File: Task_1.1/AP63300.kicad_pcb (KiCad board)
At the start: 2 copper layers, 30 x 30 mm, 14 parts, among them J1 Conn_01x03, U1 AP63300

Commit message: Fixed and updated part numbers and pcb schematics
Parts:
- C1: footprint Capacitor_SMD:C_1206_3216Metric -> Capacitor_SMD:C_1210_3225Metric
- C21, C22: footprint Capacitor_SMD:C_0201_0603Metric -> Capacitor_SMD:C_1210_3225Metric
- C3, C4: footprint Capacitor_SMD:C_0201_0603Metric -> Capacitor_SMD:C_0603_1608Metric
- R1, R2: footprint Resistor_SMD:R_0201_0603Metric -> Resistor_SMD:R_0603_1608Metric
- moved J1 7.06 mm to (28.0, 28.5)
- moved C22 5.16 mm to (42.0, 36.4)
- moved C4 5.11 mm to (38.5, 30.5)
- moved C21 4.61 mm to (42.0, 33.0)
- moved C1 3.66 mm to (31.5, 29.0)
- moved R2 2.61 mm to (38.5, 26.5)
- moved U1 2.45 mm to (35.0, 29.4)
- moved C3 2.44 mm to (35.4, 32.5)
- moved R1 1.12 mm to (38.5, 29.0)
- moved L1 0.85 mm to (35.0, 37.5)
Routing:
- net Net-(J1-Pin_3): track 28.1 -> 39.6 mm
- net Net-(J1-Pin_2): track 49.6 -> 58.1 mm
- net Net-(J1-Pin_1): track 15.8 -> 7.73 mm
- net Net-(U1-FB): track 10.1 -> 7.22 mm
- net Net-(U1-BST): track 4.20 -> 2.03 mm
- net Net-(U1-SW): track 9.30 -> 7.97 mm

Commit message: Added U1, J1 part numbers; added copper pour and vias to GND, added 3d model for L1
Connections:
- net Net-(J1-Pin_1) renamed VIN
- net Net-(J1-Pin_2) renamed GND
- net Net-(J1-Pin_3) renamed VOUT
- net Net-(U1-BST) renamed BST
- net Net-(U1-FB) renamed FB
- net Net-(U1-SW) renamed SW
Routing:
- net GND: vias 0 -> 4

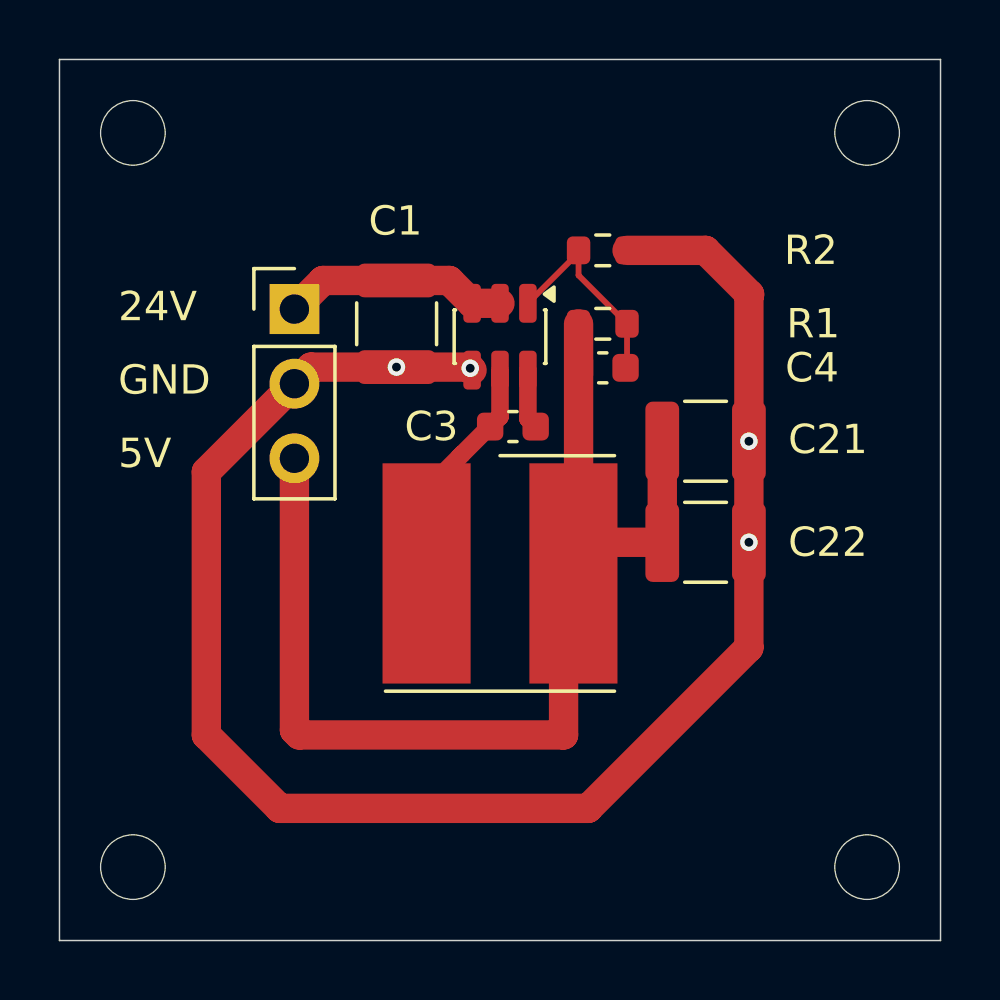
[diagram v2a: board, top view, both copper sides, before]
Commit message: added copper pour + changed inductor 3d model location
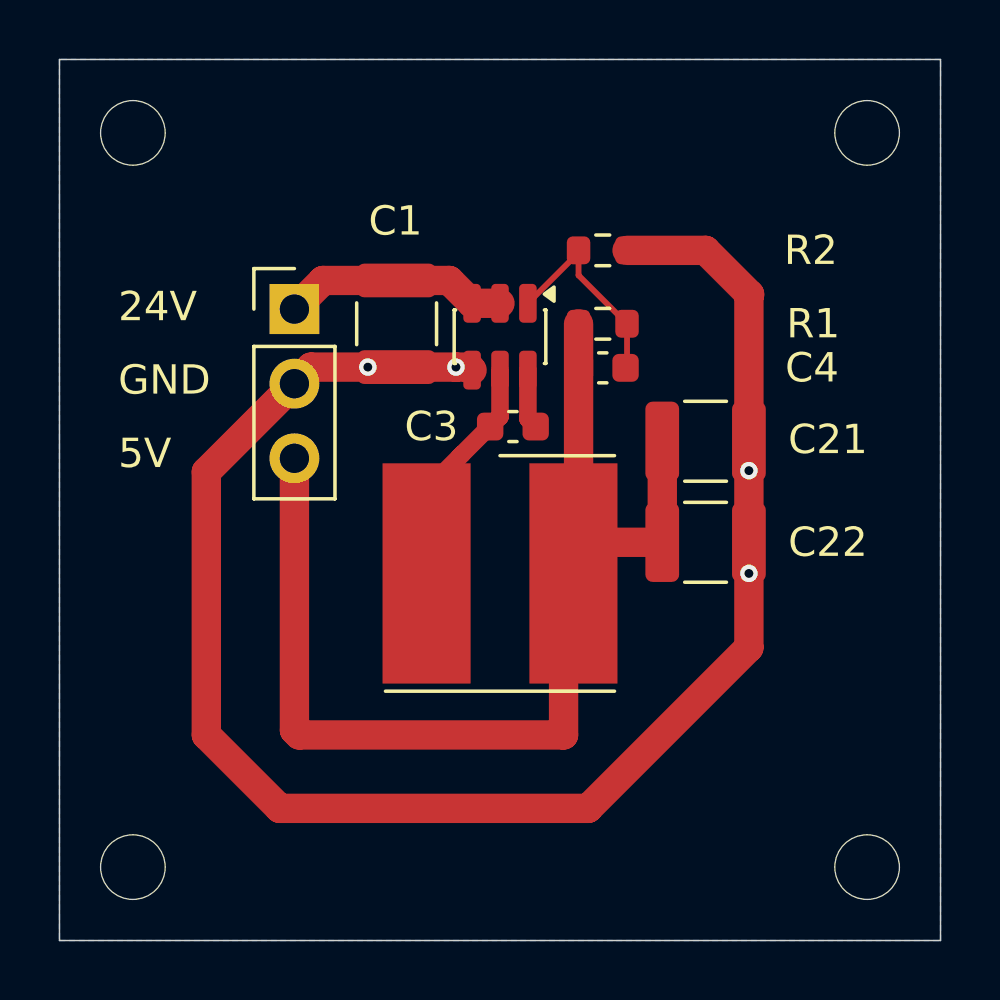
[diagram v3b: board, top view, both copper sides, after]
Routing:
- added copper zone on B.Cu, net GND
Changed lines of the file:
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@@
 		)
 		(embedded_fonts no)
-		(model "${WE_3DMODEL_DIR}/Inductor_SMD_Wurth.3dshapes/L_Wurth_WE-PD2A-7850.step"
-			(offset
-				(xyz 0 0 0)
-			)
-			(scale
-				(xyz 1 1 1)
-			)
-			(rotate
-				(xyz 0 0 0)
-			)
-		)
-		(model "C:/Users/viczi/OneDrive/Dokumentumok/KiCad_WE-PD2A (rev26b)/3dmodels/Inductor_SMD_Wurth.3dshapes/L_Wurth_WE-PD2A-7850.step"
+		(model "${KICAD10_3DMODEL_DIR}/Inductor_SMD_Wurth.3dshapes/L_Wurth_WE-PD2A-7850.step"
 			(offset
 				(xyz 0 0 0)
@@
 	)
 	(segment
-		(start 28.565 30.475)
-		(end 31.475 30.475)
+		(start 30.5 30.475)
+		(end 28.565 30.475)
+		(width 1)
+		(layer "F.Cu")
+		(net "GND")
+	)
+	(segment
+		(start 31.48 30.475)
+		(end 33.5 30.475)
 		(width 1)
 		(layer "F.Cu")
@@
 	)
 	(segment
-		(start 28 31.04)
-		(end 28.565 30.475)
+		(start 43.475 37.5)
+		(end 43.475 40.025)
 		(width 1)
 		(layer "F.Cu")
@@
 	)
 	(segment
+		(start 33.9475 30.475)
+		(end 33.98625 30.51375)
+		(width 1)
+		(layer "F.Cu")
+		(net "GND")
+	)
+	(segment
 		(start 43.5 28)
 		(end 43.475 28.025)
@@
 	)
 	(segment
+		(start 28.565 30.475)
+		(end 28 31.04)
+		(width 1)
+		(layer "F.Cu")
+		(net "GND")
+	)
+	(segment
 		(start 25 43)
 		(end 25 34.04)
@@
 	)
 	(segment
+		(start 33.5 30.475)
+		(end 33.9475 30.475)
+		(width 1)
+		(layer "F.Cu")
+		(net "GND")
+	)
+	(segment
 		(start 43.475 40.025)
 		(end 38 45.5)
@@
 	)
 	(segment
-		(start 33.9475 30.475)
-		(end 33.98625 30.51375)
-		(width 1)
-		(layer "F.Cu")
-		(net "GND")
-	)
-	(segment
-		(start 31.475 30.475)
-		(end 31.48 30.475)
-		(width 1)
-		(layer "F.Cu")
-		(net "GND")
-	)
-	(segment
 		(start 43.475 33)
+		(end 43.475 34)
+		(width 1)
+		(layer "F.Cu")
+		(net "GND")
+	)
+	(segment
+		(start 43.475 36.44)
+		(end 43.475 37.5)
+		(width 1)
+		(layer "F.Cu")
+		(net "GND")
+	)
+	(segment
+		(start 43.475 34)
 		(end 43.475 36.44)
-		(width 1)
-		(layer "F.Cu")
-		(net "GND")
-	)
-	(segment
-		(start 43.475 36.44)
-		(end 43.475 40.025)
 		(width 1)
 		(layer "F.Cu")
@@
 	(segment
 		(start 31.48 30.475)
-		(end 33.9475 30.475)
+		(end 30.5 30.475)
 		(width 1)
 		(layer "F.Cu")
@@
 	)
 	(via
-		(at 31.475 30.475)
+		(at 30.5 30.475)
 		(size 0.6)
 		(drill 0.3)
@@
 	)
 	(via
-		(at 43.475 36.44)
+		(at 33.5 30.475)
 		(size 0.6)
 		(drill 0.3)
@@
 	)
 	(via
-		(at 33.98625 30.51375)
+		(at 43.475 34)
 		(size 0.6)
 		(drill 0.3)
@@
 	)
 	(via
-		(at 43.475 33)
+		(at 43.475 37.5)
 		(size 0.6)
 		(drill 0.3)
@@
 		(net "SW")
 	)
+	(zone
+		(net "GND")
+		(layer "B.Cu")
+		(hatch edge 0.5)
+		(connect_pads thru_hole_only
+			(clearance 0.5)
+		)
+		(min_thickness 0.25)
+		(fill yes
+			(thermal_gap 0.5)
+			(thermal_bridge_width 0.5)
+			(island_removal_mode 0)
+		)
+		(polygon
+			(pts
+				(xy 20 20) (xy 20 50) (xy 50 50) (xy 50 20)
+			)
+		)
+	)
 	(generated
